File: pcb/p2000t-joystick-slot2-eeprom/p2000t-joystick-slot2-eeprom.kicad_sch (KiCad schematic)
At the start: 47 parts, among them J1 PLAYER1, J2 P2000T Port 2, J3 PLAYER2, SW1 SW_DIP_x02, U1 74HC02, U2 74HC74, U3 74HC138, U4 SST39SF010

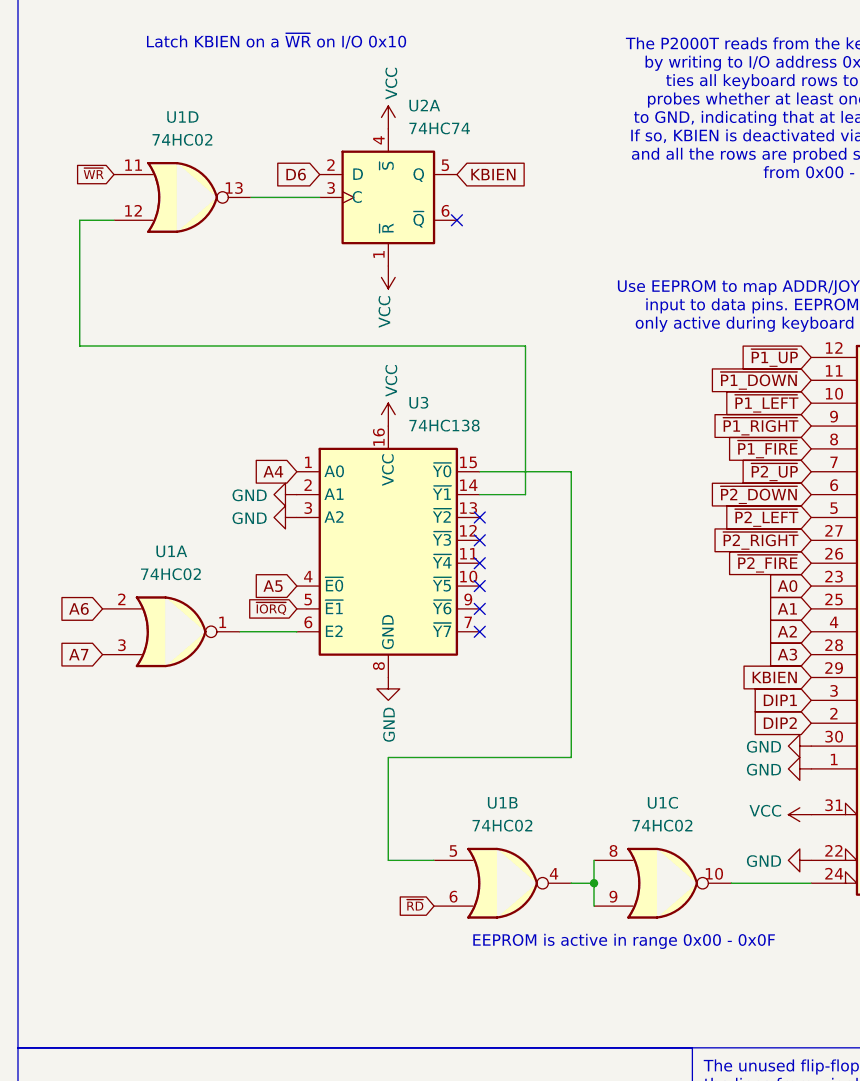
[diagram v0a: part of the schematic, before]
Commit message: Fixing design and CUPL
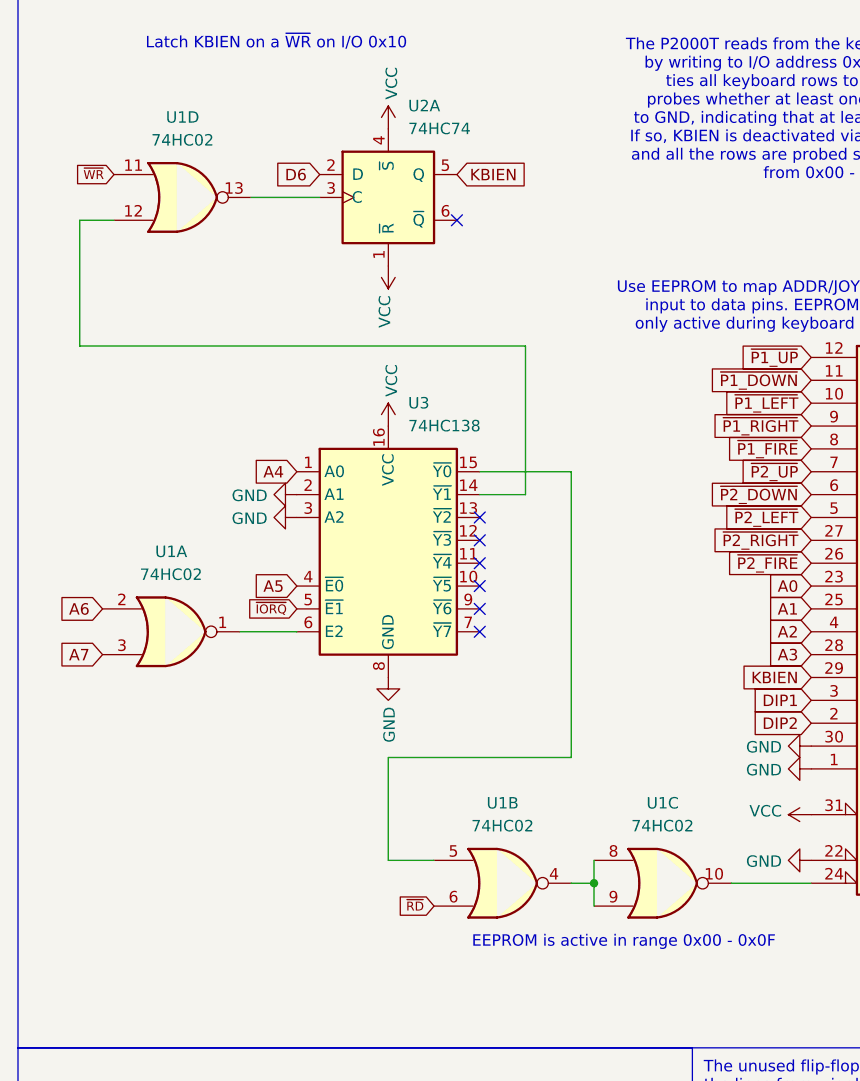
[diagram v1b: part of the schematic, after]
